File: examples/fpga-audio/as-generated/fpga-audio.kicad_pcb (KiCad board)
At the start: 2 copper layers, 100 x 84 mm, 29 parts, among them J1 3V3 IN, J2 AUDIO OUT, J3 SPI PROG, U1 iCE40UP5K, U2 PCM5102A, U3 AP2112K-1.2, U4 W25Q32JV, X1 12MHz

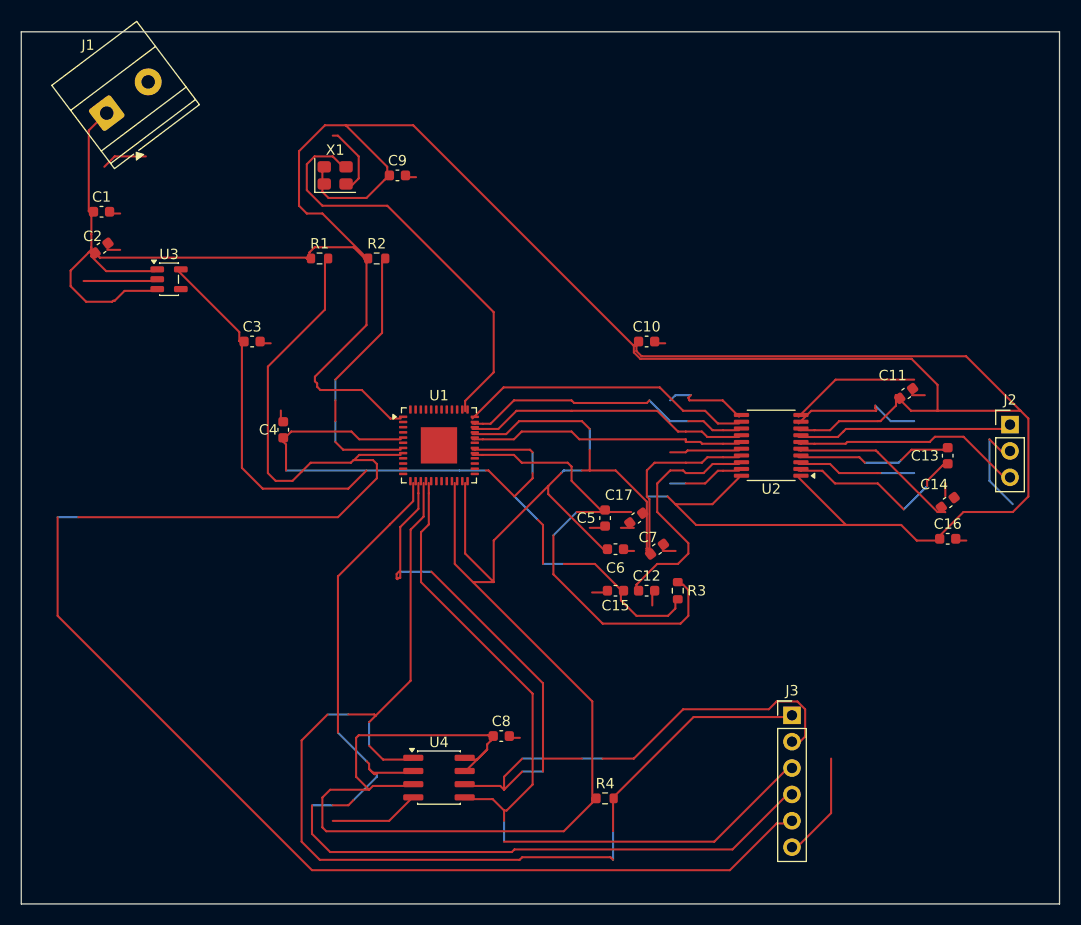
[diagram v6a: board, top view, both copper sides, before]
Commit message: Put the vias back where the copper moved, and let the fillets vote
The FPGA board came back from its re-route with two unconnected nets and
three dangling ends, and the cause was older than anything this round
added. The router hands back a via for every layer change; six passes
then reshape the copper - snapping to 45s, chamfering, spreading folds,
and now filleting - and none of them move the holes underneath. A joint
that slides a millimetre from its via is two loose ends and one broken
net, and `_unlooped` then swept the via away as orphaned, because it
kept a via only when a track ended on its exact coordinate.

Two fixes, both about what "connected" means. A via lives if kept copper
*touches* it, not if a coordinate matches. And a new `_joined` pass
re-derives the joints from the copper that actually got written: where a
net ends on two layers at one point with no via reaching it, one goes
back in. It reads the finished geometry, so it cannot drift the way six
separate passes carrying vias along with them would.

The same reasoning fixes two rules that had been measuring coordinates
rather than copper. `route.stub` matched a track end to a via's centre
exactly, and called a joint a stub whenever a reshaping pass had moved
it a quarter of a millimetre inside the very barrel it was connected to.
`route.width_step` walked a neck back to its pad and stopped at the
first width change - which, on a filleted board, is the teardrop, so
every escape's neck stopped being recognised as one.

While the three copies of the post-route pipeline were being edited for
the third time this session, they became one function. That is how
`_teardrops` had come to run on two of the three exits.

All five boards: DRC clean on both matrix versions, nothing unconnected.
Four pass their gates; the FPGA board is down to the two-layer bill it
has always had - four nets over plane cuts and one 88 degree corner.

Co-Authored-By: Claude Fable 5 <noreply@anthropic.com>
Claude-Session: https:/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
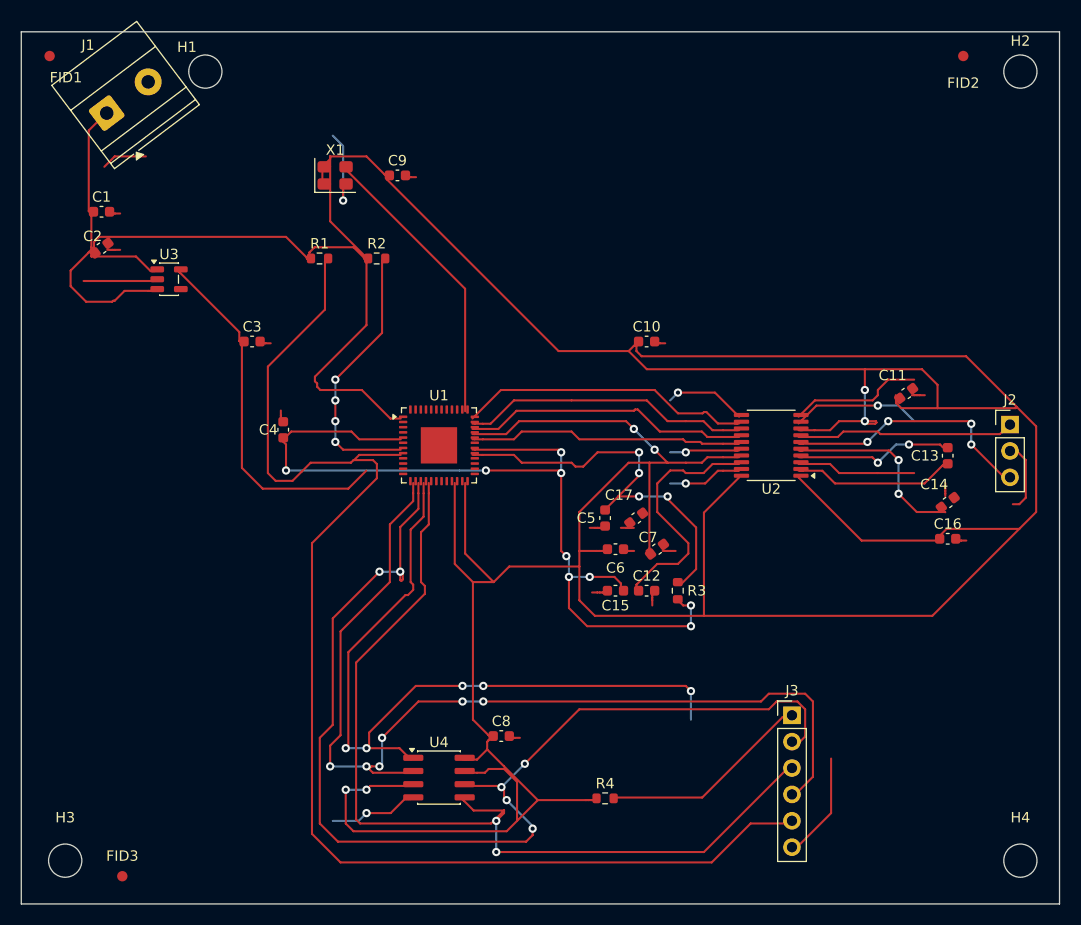
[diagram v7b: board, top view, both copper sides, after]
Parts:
- added FID1: Fiducial, Fiducial:Fiducial_1mm_Mask2mm, F.Cu at (102.7, 62.3)
- added FID2: Fiducial, Fiducial:Fiducial_1mm_Mask2mm, F.Cu at (190.7, 62.3)
- added FID3: Fiducial, Fiducial:Fiducial_1mm_Mask2mm, F.Cu at (109.7, 141.3)
- added H1: M3, MountingHole:MountingHole_3.2mm_M3, F.Cu at (117.7, 63.8)
- added H2: M3, MountingHole:MountingHole_3.2mm_M3, F.Cu at (196.2, 63.8)
- added H3: M3, MountingHole:MountingHole_3.2mm_M3, F.Cu at (104.2, 139.8)
- added H4: M3, MountingHole:MountingHole_3.2mm_M3, F.Cu at (196.2, 139.8)
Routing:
- net /CRESET: track 165.0 -> 126.3 mm
- net /SPI_SCK: track 84.5 -> 109.0 mm, vias 0 -> 6
- net /SPI_SI: track 75.5 -> 90.9 mm, vias 0 -> 2
- net /+1V2: track 108.4 -> 123.3 mm, vias 0 -> 9
- net /SPI_SS: track 107.5 -> 93.6 mm, vias 0 -> 5
- net /CLK12: track 40.5 -> 28.3 mm
- net +3V3: track 509.2 -> 500.7 mm, vias 0 -> 6
- net /VCCPLL: track 48.3 -> 41.1 mm, vias 0 -> 4
- net /OUTL: track 22.1 -> 24.7 mm, vias 0 -> 4
- net /CAPP: track 17.7 -> 15.4 mm
- net /VNEG: track 16.6 -> 18.5 mm, vias 0 -> 2
- net GND: track 124.9 -> 123.1 mm, vias 0 -> 6
- net /CAPM: track 14.9 -> 15.3 mm, vias 0 -> 2
- net /SPI_SO: vias 0 -> 6
- net /CDONE: vias 0 -> 4

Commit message: Walk the whole edge for a screw hole, and land a joint on its own pad
The fastener clearance was right and the search was not: it slid along two
edges from each corner and gave up, so boards that had had four screw holes
came back with one. It now walks a ring round the board at the inset the
screw needs, taking the nearest free point to each corner - and only from
that corner's own quarter, because a search that asked for the nearest free
point anywhere put three of the four along one edge, each of them the nearest
thing to a different corner. A quarter with no room gives no screw: three
that hold the board flat beat four that hold one side.

A pin header asks for nothing above its courtyard - the socket that fits it
lands inside the outline the header already draws - while a screw terminal's
wires leave horizontally from its face. Treating the two alike is what left a
carrier lined with headers with two holes on one edge. Both the generator and
the rule now tell them apart by footprint.

_landed folds a via that sits beside a plated hole of its own net onto the
hole. The plating already joins the faces, so the via bought nothing and cost
hole-to-hole: two drills a millimetre apart leave 0.15 mm of laminate at a
0.25 mm rule, which is what DRC reported on the opamp board.

The fillets move to the end of the pipeline. A taper is built against the end
of a run, and _landed moves ends, so a teardrop laid before it pointed at
where the run used to stop - a nought-degree corner in the angle rule.

buck-5v, motor-driver, pico-carrier, opamp-filter: 0 errors, 0 warnings.

Co-Authored-By: Claude Fable 5 <noreply@anthropic.com>
Claude-Session: https://claude.ai/code/session_01DUj7Ltu92tWg159mCSacwY
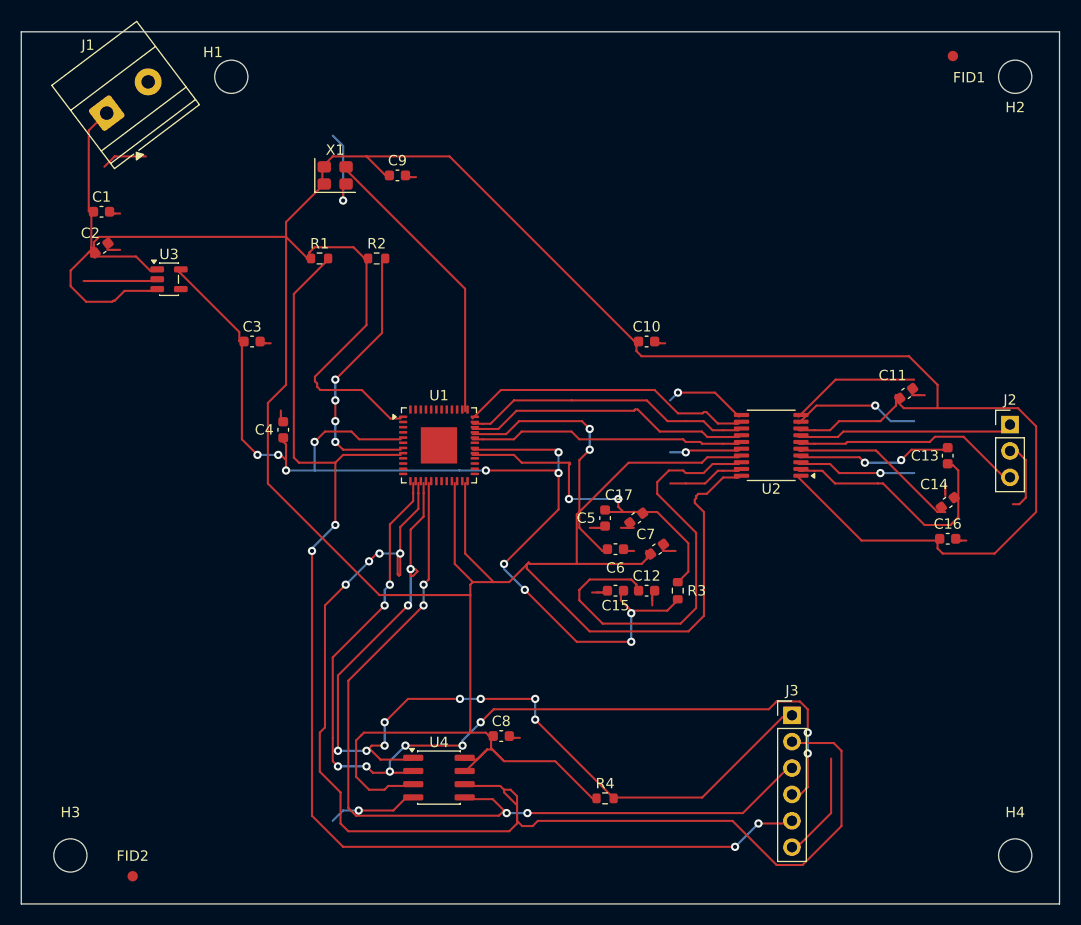
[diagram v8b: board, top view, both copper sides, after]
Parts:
- removed FID3: Fiducial, Fiducial:Fiducial_1mm_Mask2mm
- moved FID2 112.4 mm to (110.7, 141.3)
- moved FID1 87.0 mm to (189.7, 62.3)
- moved H1 2.55 mm to (120.2, 64.3)
- moved H2 0.71 mm to (195.7, 64.3)
- moved H3 0.71 mm to (104.7, 139.3)
- moved H4 0.71 mm to (195.7, 139.3)
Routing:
- net +3V3: track 500.7 -> 467.0 mm, vias 6 -> 2
- net /LDOO: track 23.9 -> 43.2 mm
- net /CRESET: track 126.3 -> 114.2 mm, vias 0 -> 4
- net /SPI_SCK: track 109.0 -> 120.5 mm, vias 6 -> 4
- net /+1V2: track 123.3 -> 112.0 mm, vias 9 -> 11
- net /CAPP: track 15.4 -> 23.8 mm
- net /SPI_SI: track 90.9 -> 83.9 mm, vias 2 -> 4
- net /VCCPLL: track 41.1 -> 34.7 mm, vias 4 -> 2
- net /SPI_SO: track 96.4 -> 92.0 mm, vias 6 -> 10
- net /OUTL: track 24.7 -> 22.1 mm, vias 4 -> 0
- net /SPI_SS: track 93.6 -> 91.5 mm, vias 5 -> 10
- net /VNEG: track 18.5 -> 16.6 mm, vias 2 -> 0
